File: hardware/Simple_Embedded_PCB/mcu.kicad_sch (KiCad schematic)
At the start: 30 parts, among them J1 USB_B_Micro, J2 SWD Connector, J3 Conn_01x09, J4 Conn_01x09, J5 Conn_01x09, J6 Conn_01x09, Q1 AO3400A, U1 STM32F103C8Tx, X1 SG-8018CE 8.000000MHz

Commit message: Added JLCPCB part numbers
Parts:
- C1: LCSC Part Number (none) -> C440198
- C2, C3, C4, C5, C7, C9: LCSC Part Number (none) -> C307331
- C6: LCSC Part Number (none) -> C15195
- C8: LCSC Part Number (none) -> C15849
- D1: LCSC Part Number (none) -> C8678
- D2: LCSC Part Number (none) -> C2297
- J1: LCSC Part Number (none) -> C132563
- J2: LCSC Part Number (none) -> C598540
- Q1: LCSC Part Number (none) -> C20917
- R1, R2, R3, R4: LCSC Part Number (none) -> C25900
- R5, R6, R9: LCSC Part Number (none) -> C25744
- R7: LCSC Part Number (none) -> C25091
- R8: LCSC Part Number (none) -> C23025
- S1: LCSC Part Number (none) -> C318884
- U1: LCSC Part Number (none) -> C8734
- X1: LCSC Part Number (none) -> C390495
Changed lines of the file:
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@@
+      (effects (font (size 1.27 1.27)) hide)
+    )
+    (property "LCSC Part Number" "C8734" (id 4) (at 156.21 85.09 0)
       (effects (font (size 1.27 1.27)) hide)
     )
@@
       (effects (font (size 1.27 1.27)) hide)
     )
+    (property "LCSC Part Number" "C25900" (id 4) (at 29.21 137.16 0)
+      (effects (font (size 1.27 1.27)) hide)
+    )
     (pin "1")
     (pin "2")
@@
     )
     (property "Datasheet" "~" (id 3) (at 189.23 41.91 0)
+      (effects (font (size 1.27 1.27)) hide)
+    )
+    (property "LCSC Part Number" "C15849" (id 4) (at 189.23 41.91 0)
       (effects (font (size 1.27 1.27)) hide)
     )
@@
       (effects (font (size 1.27 1.27)) hide)
     )
+    (property "LCSC Part Number" "C25900" (id 4) (at 87.63 137.16 0)
+      (effects (font (size 1.27 1.27)) hide)
+    )
     (pin "1")
     (pin "2")
@@
     )
     (property "Datasheet" "~" (id 3) (at 252.73 130.81 0)
+      (effects (font (size 1.27 1.27)) hide)
+    )
+    (property "LCSC Part Number" "C307331" (id 4) (at 252.73 130.81 0)
       (effects (font (size 1.27 1.27)) hide)
     )
@@
     )
     (property "Datasheet" "~" (id 3) (at 119.38 60.96 0)
+      (effects (font (size 1.27 1.27)) hide)
+    )
+    (property "LCSC Part Number" "C25744" (id 4) (at 119.38 60.96 0)
       (effects (font (size 1.27 1.27)) hide)
     )
@@
       (effects (font (size 1.27 1.27)) hide)
     )
+    (property "LCSC Part Number" "C8678" (id 4) (at 48.26 82.55 0)
+      (effects (font (size 1.27 1.27)) hide)
+    )
     (pin "1")
     (pin "2")
@@
     )
     (property "Datasheet" "~" (id 3) (at 39.37 137.16 0)
+      (effects (font (size 1.27 1.27)) hide)
+    )
+    (property "LCSC Part Number" "C25900" (id 4) (at 39.37 137.16 0)
       (effects (font (size 1.27 1.27)) hide)
     )
@@
       (effects (font (size 1.27 1.27)) hide)
     )
+    (property "LCSC Part Number" "C390495" (id 4) (at 243.84 144.78 0)
+      (effects (font (size 1.27 1.27)) hide)
+    )
     (pin "1")
     (pin "2")
@@
       (effects (font (size 1.27 1.27)) hide)
     )
+    (property "LCSC Part Number" "C307331" (id 4) (at 142.24 41.91 0)
+      (effects (font (size 1.27 1.27)) hide)
+    )
     (pin "1")
     (pin "2")
@@
       (effects (font (size 1.27 1.27)) hide)
     )
+    (property "LCSC Part Number" "C25744" (id 4) (at 190.5 110.49 0)
+      (effects (font (size 1.27 1.27)) hide)
+    )
     (pin "1")
     (pin "2")
@@
     )
     (property "Datasheet" "~" (id 3) (at 96.52 41.91 0)
+      (effects (font (size 1.27 1.27)) hide)
+    )
+    (property "LCSC Part Number" "C440198" (id 4) (at 96.52 41.91 0)
       (effects (font (size 1.27 1.27)) hide)
     )
@@
       (effects (font (size 1.27 1.27)) hide)
     )
+    (property "LCSC Part Number" "C20917" (id 4) (at 204.47 105.41 0)
+      (effects (font (size 1.27 1.27)) hide)
+    )
     (pin "1")
     (pin "2")
@@
       (effects (font (size 1.27 1.27)) hide)
     )
+    (property "LCSC Part Number" "C25900" (id 4) (at 97.79 137.16 0)
+      (effects (font (size 1.27 1.27)) hide)
+    )
     (pin "1")
     (pin "2")
@@
     )
     (property "Datasheet" "~" (id 3) (at 231.14 139.7 0)
+      (effects (font (size 1.27 1.27)) hide)
+    )
+    (property "LCSC Part Number" "C25744" (id 4) (at 231.14 139.7 0)
       (effects (font (size 1.27 1.27)) hide)
     )
@@
       (effects (font (size 1.27 1.27)) hide)
     )
+    (property "LCSC Part Number" "C2297" (id 4) (at 207.01 93.98 0)
+      (effects (font (size 1.27 1.27)) hide)
+    )
     (pin "1")
     (pin "2")
@@
     )
     (property "Datasheet" "~" (id 3) (at 107.95 41.91 0)
+      (effects (font (size 1.27 1.27)) hide)
+    )
+    (property "LCSC Part Number" "C307331" (id 4) (at 107.95 41.91 0)
       (effects (font (size 1.27 1.27)) hide)
     )
@@
       (effects (font (size 1.27 1.27)) hide)
     )
+    (property "LCSC Part Number" "C23025" (id 4) (at 207.01 85.09 0)
+      (effects (font (size 1.27 1.27)) hide)
+    )
     (pin "1")
     (pin "2")
@@
       (effects (font (size 1.27 1.27)) hide)
     )
+    (property "LCSC Part Number" "C307331" (id 4) (at 119.38 41.91 0)
+      (effects (font (size 1.27 1.27)) hide)
+    )
     (pin "1")
     (pin "2")
@@
     )
     (property "Datasheet" "~" (id 3) (at 130.81 41.91 0)
+      (effects (font (size 1.27 1.27)) hide)
+    )
+    (property "LCSC Part Number" "C307331" (id 4) (at 130.81 41.91 0)
       (effects (font (size 1.27 1.27)) hide)
     )
@@
       (effects (font (size 1.27 1.27)) hide)
     )
+    (property "LCSC Part Number" "C15195" (id 4) (at 166.37 41.91 0)
+      (effects (font (size 1.27 1.27)) hide)
+    )
     (pin "1")
     (pin "2")
@@
     )
     (property "Datasheet" "~" (id 3) (at 39.37 88.9 0)
+      (effects (font (size 1.27 1.27)) hide)
+    )
+    (property "LCSC Part Number" "C132563" (id 4) (at 35.56 87.63 0)
       (effects (font (size 1.27 1.27)) hide)
     )
@@
     )
     (property "Datasheet" "~" (id 3) (at 36.83 44.45 0)
+      (effects (font (size 1.27 1.27)) hide)
+    )
+    (property "LCSC Part Number" "C598540" (id 4) (at 36.83 44.45 0)
       (effects (font (size 1.27 1.27)) hide)
     )
@@
       (effects (font (size 1.27 1.27)) (justify left bottom) hide)
     )
+    (property "LCSC Part Number" "C318884" (id 8) (at 236.22 62.23 0)
+      (effects (font (size 1.27 1.27)) hide)
+    )
     (pin "A")
     (pin "B")
@@
     )
     (property "Datasheet" "~" (id 3) (at 195.58 105.41 0)
+      (effects (font (size 1.27 1.27)) hide)
+    )
+    (property "LCSC Part Number" "C25091" (id 4) (at 195.58 105.41 0)
       (effects (font (size 1.27 1.27)) hide)
     )
@@
       (effects (font (size 1.27 1.27)) hide)
     )
+    (property "LCSC Part Number" "C307331" (id 4) (at 177.8 41.91 0)
+      (effects (font (size 1.27 1.27)) hide)
+    )

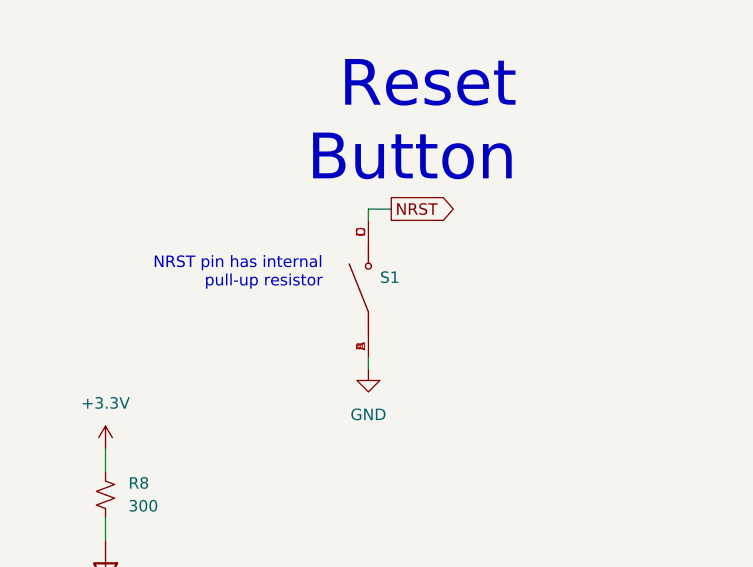
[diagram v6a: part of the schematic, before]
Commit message: Changed KiCad project to use symbols, footprints, and 3D models from project itself.
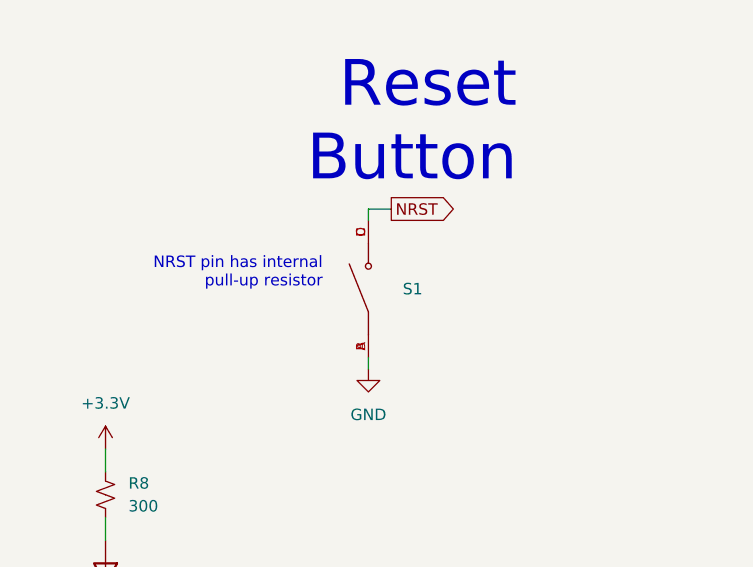
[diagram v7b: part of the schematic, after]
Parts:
- J2: footprint MySO:Amphenol-20021121-0-0-0 -> Simple_Embedded_PCB:Amphenol-20021121-0-0-0
- S1: footprint MySO:SW_TS-1187A-B-A-B -> Simple_Embedded_PCB:SW_TS-1187A-B-A-B; symbol TS-1187A-B-A-B:TS-1187A-B-A-B -> Simple_Embedded_PCB:TS-1187A-B-A-B; LCSC Part Number C318884 -> (none); MANUFACTURER XKB Industrial Precision -> (none); MAXIMUM_PACKAGE_HEIGHT 1.5mm -> (none); PARTREV A0 -> (none); STANDARD Manufacturer Recommendations -> (none)
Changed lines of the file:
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@@
     (property "Reference" "J2" (id 0) (at 38.1 33.02 0))
     (property "Value" "SWD Connector" (id 1) (at 38.1 35.56 0))
-    (property "Footprint" "MySO:Amphenol-20021121-0-0-0" (id 2) (at 36.83 44.45 0)
+    (property "Footprint" "Simple_Embedded_PCB:Amphenol-20021121-0-0-0" (id 2) (at 36.83 44.45 0)
       (effects (font (size 1.27 1.27)) hide)
     )
@@
     (pin "9")
   )
-  (symbol (lib_id "TS-1187A-B-A-B:TS-1187A-B-A-B") (at 236.22 62.23 90) (unit 1)
-    (in_bom yes) (on_board yes) (fields_autoplaced)
-    (property "Reference" "S1" (id 0) (at 237.49 60.9599 90)
+  (symbol (lib_id "Simple_Embedded_PCB:TS-1187A-B-A-B") (at 236.22 62.23 90) (unit 1)
+    (in_bom yes) (on_board yes)
+    (property "Reference" "S1" (id 0) (at 240.03 62.23 90)
       (effects (font (size 1.27 1.27)) (justify right))
     )
-    (property "Value" "TS-1187A-B-A-B" (id 1) (at 237.49 63.4999 90)
-      (effects (font (size 1.27 1.27)) (justify right) hide)
+    (property "Value" "TS-1187A-B-A-B" (id 1) (at 238.76 64.77 0)
+      (effects (font (size 1.27 1.27)) (justify left bottom) hide)
     )
-    (property "Footprint" "MySO:SW_TS-1187A-B-A-B" (id 2) (at 236.22 62.23 0)
+    (property "Footprint" "Simple_Embedded_PCB:SW_TS-1187A-B-A-B" (id 2) (at 241.3 63.5 0)
       (effects (font (size 1.27 1.27)) (justify left bottom) hide)
     )
@@
       (effects (font (size 1.27 1.27)) (justify left bottom) hide)
     )
-    (property "PARTREV" "A0" (id 4) (at 236.22 62.23 0)
-      (effects (font (size 1.27 1.27)) (justify left bottom) hide)
-    )
-    (property "STANDARD" "Manufacturer Recommendations" (id 5) (at 236.22 62.23 0)
-      (effects (font (size 1.27 1.27)) (justify left bottom) hide)
-    )
-    (property "MAXIMUM_PACKAGE_HEIGHT" "1.5mm" (id 6) (at 236.22 62.23 0)
-      (effects (font (size 1.27 1.27)) (justify left bottom) hide)
-    )
-    (property "MANUFACTURER" "XKB Industrial Precision" (id 7) (at 236.22 62.23 0)
-      (effects (font (size 1.27 1.27)) (justify left bottom) hide)
-    )
-    (property "LCSC Part Number" "C318884" (id 8) (at 236.22 62.23 0)
-      (effects (font (size 1.27 1.27)) hide)
-    )
     (pin "A")
